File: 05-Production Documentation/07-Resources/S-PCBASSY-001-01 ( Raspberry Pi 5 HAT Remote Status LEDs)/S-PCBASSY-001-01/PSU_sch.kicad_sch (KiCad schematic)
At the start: 16 parts, among them J1 GPIO, Q4 AO3401A, U1 CAT24C256

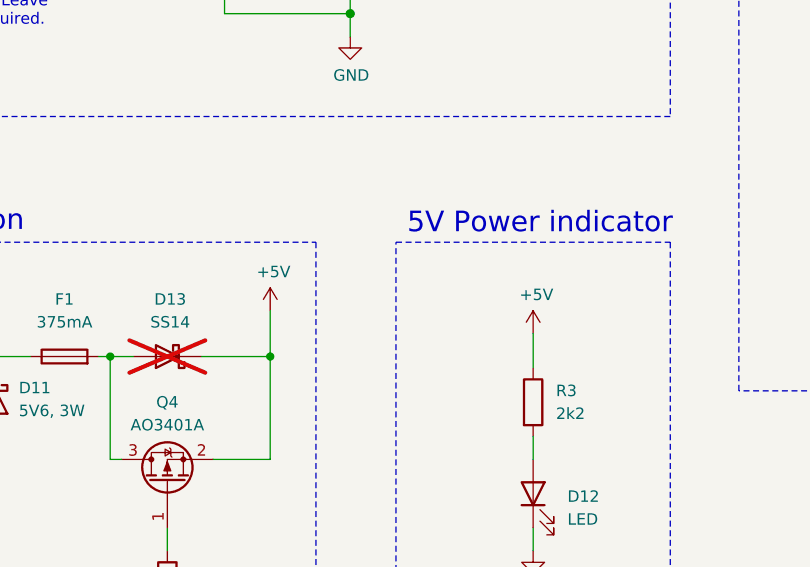
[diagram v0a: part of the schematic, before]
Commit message: PCB Routing done
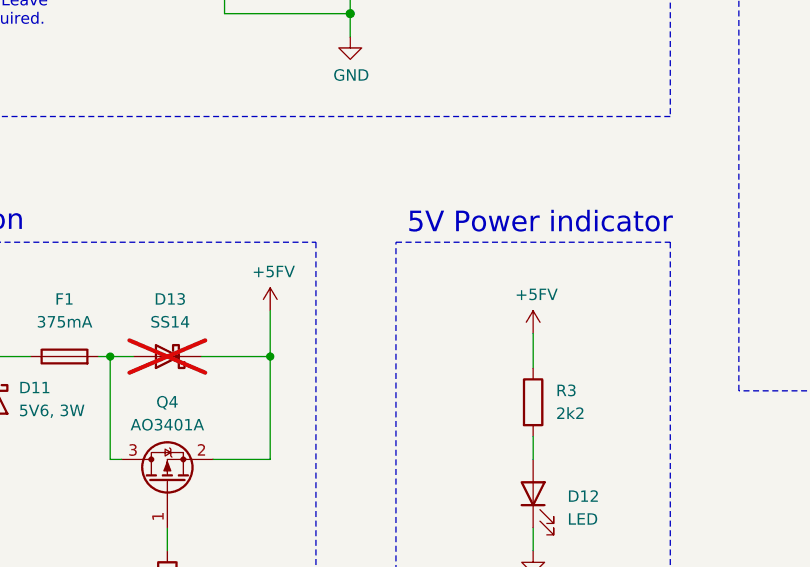
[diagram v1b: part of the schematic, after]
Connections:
- net +5V: no longer D13.1 (K), Q4.2 (S), R3.1
- new net +5FV: D13.1 (K), Q4.2 (S), R3.1
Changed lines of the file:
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@@
 			)
 		)
-		(property "Value" "+5V"
+		(property "Value" "+5FV"
 			(at 103.2383 117.5956 0)
 			(effects
@@
 			)
 		)
-		(property "Value" "+5V"
+		(property "Value" "+5FV"
 			(at 132.4483 120.1356 0)
 			(effects
